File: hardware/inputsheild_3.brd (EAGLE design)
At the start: 71.1 x 90 mm, 57 parts

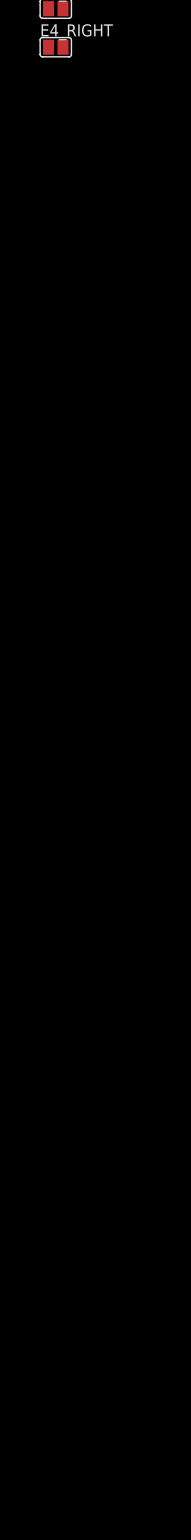
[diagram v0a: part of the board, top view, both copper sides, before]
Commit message: so many jumpers in schematic
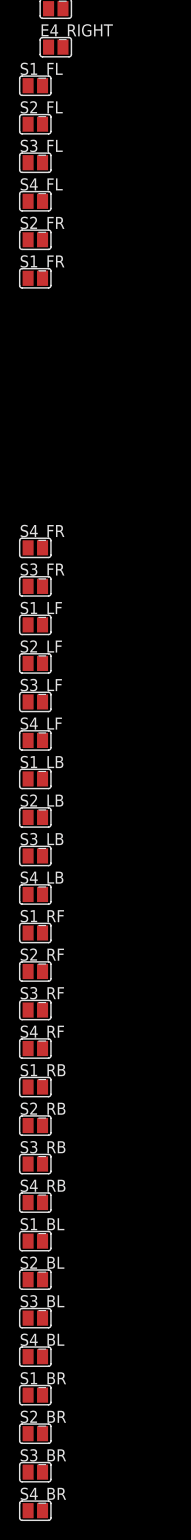
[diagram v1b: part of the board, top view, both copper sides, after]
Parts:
- added S1_BL, S1_BR, S1_FL, S1_FR, S1_LB, S1_LF, S1_RB, S1_RF, S2_BL, S2_BR, S2_FL, S2_FR, S2_LB, S2_LF, S2_RB, S2_RF, S3_BL, S3_BR, S3_FL, S3_FR, S3_LB, S3_LF, S3_RB, S3_RF, S4_BL, S4_BR, S4_FL, S4_FR, S4_LB, S4_LF, S4_RB, S4_RF: (no value), jumper:SJ
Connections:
- new net S1: S1_BL.1, S1_BR.1, S1_FL.1, S1_FR.1, S1_LB.1, S1_LF.1, S1_RB.1, S1_RF.1
- new net S2: S2_BL.1, S2_BR.1, S2_FL.1, S2_FR.1, S2_LB.1, S2_LF.1, S2_RB.1, S2_RF.1
- new net S3: S3_BL.1, S3_BR.1, S3_FL.1, S3_FR.1, S3_LB.1, S3_LF.1, S3_RB.1, S3_RF.1
- new net S4: S4_BL.1, S4_BR.1, S4_FL.1, S4_FR.1, S4_LB.1, S4_LF.1, S4_RB.1, S4_RF.1
- new net SBL: S1_BL.2, S2_BL.2, S3_BL.2, S4_BL.2
- new net SBR: S1_BR.2, S2_BR.2, S3_BR.2, S4_BR.2
- new net SFL: S1_FL.2, S2_FL.2, S3_FL.2, S4_FL.2
- new net SFR: S1_FR.2, S2_FR.2, S3_FR.2, S4_FR.2
- new net SLB: S1_LB.2, S2_LB.2, S3_LB.2, S4_LB.2
- new net SLF: S1_LF.2, S2_LF.2, S3_LF.2, S4_LF.2
- new net SRB: S1_RB.2, S2_RB.2, S3_RB.2, S4_RB.2
- new net SRF: S1_RF.2, S2_RF.2, S3_RF.2, S4_RF.2

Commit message: wooo
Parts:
- removed E1_FRONT, E2_FRONT, E3_FRONT, E4_FRONT: (no value), jumper:SJ
- added E1_FRNT, E2_FRNT, E3_FRNT, E4_FRNT: (no value), jumper:SJ
- moved S2_BR 290.6 mm to (51.1, 49.2), flipped to the bottom
- moved S2_BL 279.5 mm to (51.1, 52.9), flipped to the bottom
- moved S1_BR 274.1 mm to (20.4, 48.9), flipped to the bottom
- moved S2_RB 268.5 mm to (51.1, 56.7), flipped to the bottom
- moved S3_BR 267.6 mm to (51.1, 19.1), flipped to the bottom
- moved S1_BL 262.4 mm to (20.2, 52.6), flipped to the bottom
- moved S4_BR 257.8 mm to (20.6, 19.1), flipped to the bottom
- moved S2_RF 257.6 mm to (51.1, 60.5), flipped to the bottom
- moved S3_BL 256.8 mm to (51.1, 22.9), flipped to the bottom
- moved S1_RB 250.7 mm to (20.0, 56.3), flipped to the bottom
- moved S2_LB 247.0 mm to (51.1, 64.2), flipped to the bottom
- moved S4_BL 246.3 mm to (20.6, 22.8), flipped to the bottom
- moved S3_RB 246.1 mm to (51.1, 26.6), flipped to the bottom
- moved S1_RF 239.2 mm to (19.8, 60.1), flipped to the bottom
- moved S2_LF 236.4 mm to (51.1, 68.0), flipped to the bottom
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- renumbered PAD1 to GND_, PAD10 to SLF_, PAD11 to SLB_, PAD12 to SBL_, PAD13 to SRF_, PAD14 to SRB_, PAD15 to SFR_, PAD16 to 5V_, PAD17 to GND, PAD18 to EF, PAD19 to EL, PAD2 to EF_, PAD20 to ER, PAD21 to EB, PAD22 to TRG, PAD23 to A4, PAD24 to A5, PAD25 to SFL, PAD26 to SLF, PAD27 to SLB, PAD28 to SBL, PAD29 to SRF, PAD3 to EL_, PAD30 to SRB, PAD31 to SFR, PAD32 to 5V, PAD4 to ER_, PAD5 to EB_, PAD6 to TRG_, PAD7 to A4_, PAD8 to A5_, PAD9 to SFL_
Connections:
- removed net D12: B1.D12
- removed net D2: B1.D2
- removed net D3: B1.D3
- removed net D4: B1.D4
- removed net D5: B1.D5
- removed net D6: B1.D6
- new net A4: A4.1, A4_.1, B1.A4
- new net A5: A5.1, A5_.1, B1.A5
- net +5V: now also 5V.1, 5V_.1
- net E1: now also E1_FRNT.1; no longer E1_FRONT.1
- net E2: now also E2_FRNT.1; no longer E2_FRONT.1
- net E3: now also E3_FRNT.1; no longer E3_FRONT.1
- net E4: now also E4_FRNT.1; no longer E4_FRONT.1
- net EB: now also EB.1, EB_.1
- net EF: now also E1_FRNT.2, E2_FRNT.2, E3_FRNT.2, E4_FRNT.2, EF.1, EF_.1; no longer E1_FRONT.2, E2_FRONT.2, E3_FRONT.2, E4_FRONT.2
- net EL: now also EL.1, EL_.1
- net ER: now also ER.1, ER_.1
- net GND: now also B1.GND@1, B1.GND@2, GND.1, GND_.1
- net S1: now also SWITCH_1.2
- net S2: now also SWITCH_2.2
- net S3: now also SWITCH_3.2
- net S4: now also SWITCH_4.2
- net SBL: now also B1.D3, SBL.1, SBL_.1
- net SBR: now also B1.A0
- net SFL: now also B1.D2, SFL.1, SFL_.1
- net SFR: now also B1.A1, B1.D5, SFR.1, SFR_.1
- net SLB: now also SLB.1, SLB_.1
- net SLF: now also B1.D4, SLF.1, SLF_.1
- net SRB: now also B1.D12, SRB.1, SRB_.1
- net SRF: now also B1.D6, SRF.1, SRF_.1
- net TRIG: now also TRG.1, TRG_.1
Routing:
- net S4: track 0.00 -> 39.6 mm
- net S1: track 0.00 -> 36.0 mm
- net S3: track 0.00 -> 34.6 mm
- net S2: track 0.00 -> 26.2 mm
- net E1: track 0.00 -> 23.0 mm
- net E3: track 0.00 -> 21.5 mm
- net E4: track 0.00 -> 21.3 mm
- net E2: track 0.00 -> 20.4 mm
